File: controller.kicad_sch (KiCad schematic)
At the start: 19 parts, among them U4 STM32H742VGTx

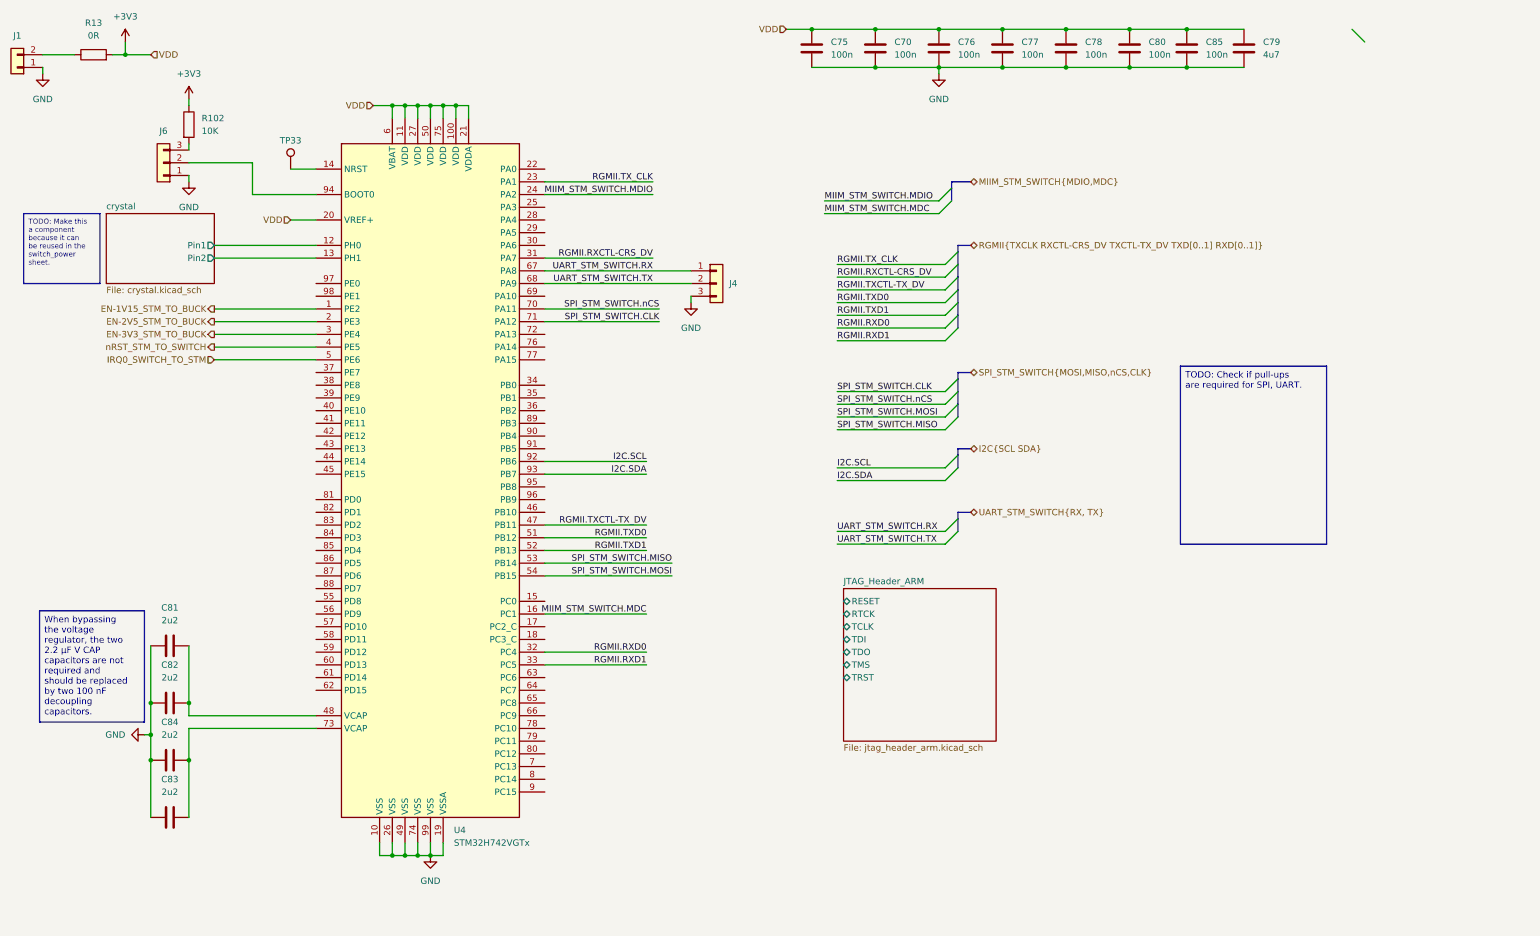
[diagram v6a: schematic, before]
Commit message: connects RGMII1 bus between Switch and STM. Refs: #1
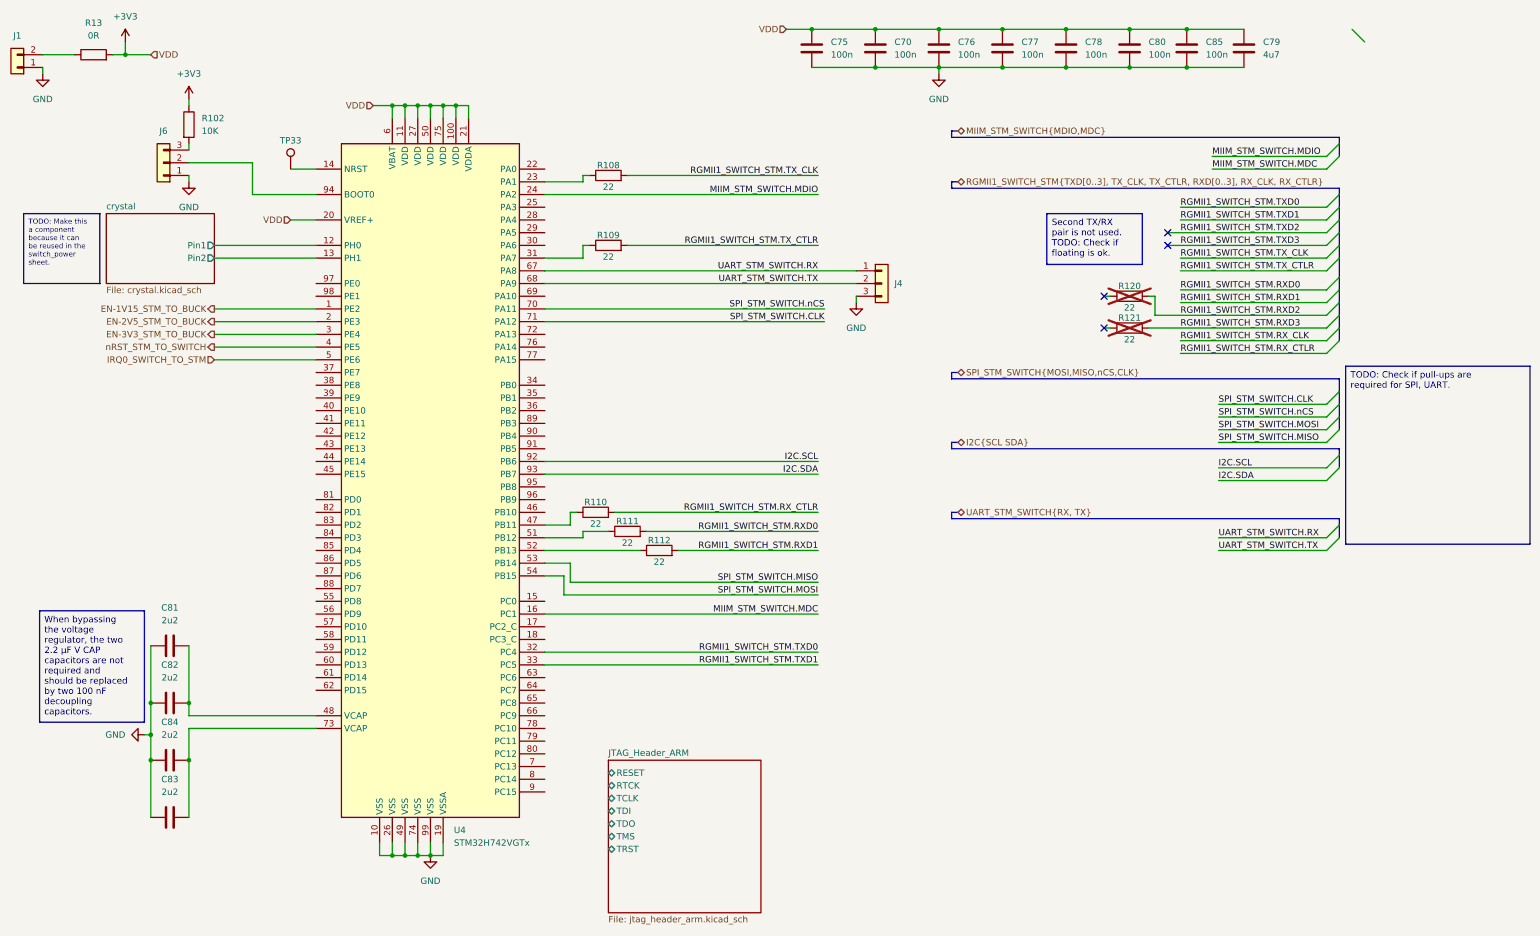
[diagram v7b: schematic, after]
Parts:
- added R108, R109, R110, R111, R112, R120, R121: 22, KL_Footprints:R_0603, symbol KL_R:R_22_100mW_1pct_0603
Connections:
- net RGMII.RXCTL-CRS_DV: no longer names the net of U4.31 (PA7)
- net RGMII.RXCTL-CRS_DV: now also R109.1
- net RGMII.RXD0 renamed RGMII1_SWITCH_STM.TXD0
- net RGMII.RXD1 renamed RGMII1_SWITCH_STM.TXD1
- net RGMII.TXCTL-TX_DV: no longer names the net of U4.47 (PB11)
- net RGMII.TXCTL-TX_DV: now also R110.1
- net RGMII.TXD0: no longer names the net of U4.51 (PB12)
- net RGMII.TXD0: now also R111.1
- net RGMII.TXD1: no longer names the net of U4.52 (PB13)
- net RGMII.TXD1: now also R112.1
- net RGMII.TX_CLK: no longer names the net of U4.23 (PA1)
- net RGMII.TX_CLK: now also R108.1
- new net RGMII1_SWITCH_STM.RXD0: R111.2
- new net RGMII1_SWITCH_STM.RXD1: R112.2
- new net RGMII1_SWITCH_STM.RXD2: R120.2
- new net RGMII1_SWITCH_STM.RXD3: R121.2
- new net RGMII1_SWITCH_STM.RX_CTLR: R110.2
- new net RGMII1_SWITCH_STM.TX_CLK: R108.2
- new net RGMII1_SWITCH_STM.TX_CTLR: R109.2
- no-connect marks 0 -> 4
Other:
- moved on the sheet: J4

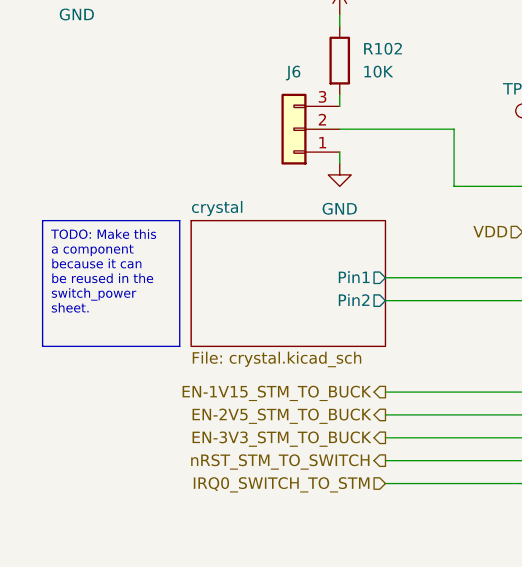
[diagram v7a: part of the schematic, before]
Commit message: Uses crystal sheet in all places. Refs: #1
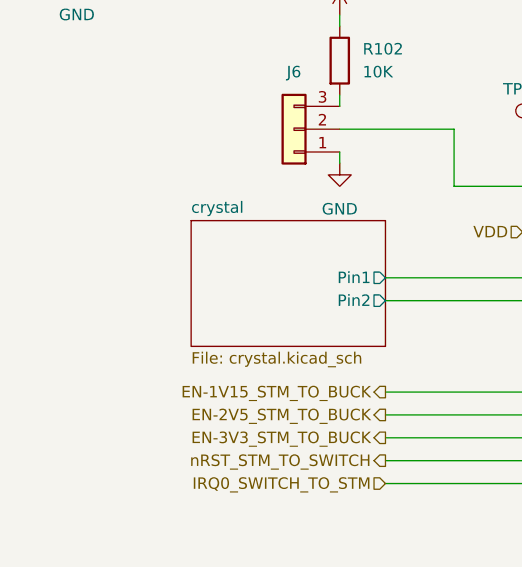
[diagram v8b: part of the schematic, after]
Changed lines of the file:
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@@
-		)
-	)
-	(text_box "TODO: Make this a component because it can be reused in the switch_power sheet."
-		(exclude_from_sim no)
-		(at 20.32 53.34 0)
-		(size 15.24 13.97)
-		(margins 0.9525 0.9525 0.9525 0.9525)
-		(stroke
-			(width 0)
-			(type solid)
-		)
-		(fill
-			(type none)
-		)
-		(effects
-			(font
-				(size 1.016 1.016)
-			)
-			(justify left top)
 		)
 	)
